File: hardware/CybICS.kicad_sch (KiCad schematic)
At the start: 64 parts, among them J1 Raspberry_Pi_2_3, J2 Conn_01x03_Pin, J3 Conn_01x05_Pin, SW1 SW_Push, SW2 SW_Push, U1 STM32G070RBTx

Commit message: Update on shematic and pcb design
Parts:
- C1, C2, C4: JLCPCB Part # (none) -> C38141
- C3: JLCPCB Part # (none) -> C1779
- D1, D14, D16, D18, D5, D6: JLCPCB Part # (none) -> C434438
- D10, D3: JLCPCB Part # (none) -> C434440
- D11, D12, D13, D15, D17, D19, D2, D4, D8: JLCPCB Part # (none) -> C434442
- D7, D9: JLCPCB Part # (none) -> C434441
- DS1: JLCPCB Part # (none) -> C5307341
- J1: JLCPCB Part # (none) -> C5224014
- J2: JLCPCB Part # (none) -> C168677
- J3: JLCPCB Part # (none) -> C225257
- R1, R10, R11, R12, R2, R20, R21, R22, R23, R24, R25, R26, R3, R4, R5, R6, R7, R8, R9: JLCPCB Part # (none) -> C17408
- R13, R14, R15, R16, R17, R18, R19: JLCPCB Part # (none) -> C304192
- R27: JLCPCB Part # (none) -> C17513
- RV1: JLCPCB Part # (none) -> C36376
- SW1, SW2: JLCPCB Part # (none) -> C428628
- U1: JLCPCB Part # (none) -> C529340

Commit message: first rapid prototype phase finished
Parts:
- FID1, FID2, FID3, H1, H2, H3: now left out of the parts list
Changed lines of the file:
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@@
     )
   )
-  (symbol (lib_id "Mechanical:Fiducial") (at 16.51 190.5 0) (unit 1)
-    (in_bom yes) (on_board yes) (dnp no) (fields_autoplaced)
+  (symbol (lib_name "Fiducial_1") (lib_id "Mechanical:Fiducial") (at 16.51 190.5 0) (unit 1)
+    (in_bom no) (on_board yes) (dnp no) (fields_autoplaced)
     (property "Reference" "FID1" (at 19.05 189.23 0)
       (effects (font (size 1.27 1.27)) (justify left))
@@
   )
   (symbol (lib_id "Mechanical:MountingHole") (at 35.56 175.26 0) (unit 1)
-    (in_bom yes) (on_board yes) (dnp no) (fields_autoplaced)
+    (in_bom no) (on_board yes) (dnp no) (fields_autoplaced)
     (property "Reference" "H2" (at 38.1 173.99 0)
       (effects (font (size 1.27 1.27)) (justify left))
@@
   )
   (symbol (lib_id "Mechanical:MountingHole") (at 16.51 175.26 0) (unit 1)
-    (in_bom yes) (on_board yes) (dnp no) (fields_autoplaced)
+    (in_bom no) (on_board yes) (dnp no) (fields_autoplaced)
     (property "Reference" "H1" (at 19.05 173.99 0)
       (effects (font (size 1.27 1.27)) (justify left))
@@
   )
   (symbol (lib_id "Mechanical:MountingHole") (at 16.51 182.88 0) (unit 1)
-    (in_bom yes) (on_board yes) (dnp no) (fields_autoplaced)
+    (in_bom no) (on_board yes) (dnp no) (fields_autoplaced)
     (property "Reference" "H3" (at 19.05 181.61 0)
       (effects (font (size 1.27 1.27)) (justify left))
@@
   )
   (symbol (lib_id "Mechanical:Fiducial") (at 44.45 190.5 0) (unit 1)
-    (in_bom yes) (on_board yes) (dnp no) (fields_autoplaced)
+    (in_bom no) (on_board yes) (dnp no) (fields_autoplaced)
     (property "Reference" "FID3" (at 46.99 189.23 0)
       (effects (font (size 1.27 1.27)) (justify left))
@@
     )
   )
-  (symbol (lib_id "Mechanical:Fiducial") (at 30.48 190.5 0) (unit 1)
-    (in_bom yes) (on_board yes) (dnp no) (fields_autoplaced)
+  (symbol (lib_name "Fiducial_2") (lib_id "Mechanical:Fiducial") (at 30.48 190.5 0) (unit 1)
+    (in_bom no) (on_board yes) (dnp no) (fields_autoplaced)
     (property "Reference" "FID2" (at 33.02 189.23 0)
       (effects (font (size 1.27 1.27)) (justify left))

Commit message: Added vscode
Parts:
- J3: JLCPCB Part # C225257 -> C225480
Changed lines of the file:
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@@
       (effects (font (size 1.27 1.27)) hide)
     )
-    (property "JLCPCB Part #" "C225257" (at 266.7 152.4 0)
+    (property "JLCPCB Part #" "C225480" (at 266.7 152.4 0)
       (effects (font (size 1.27 1.27)) hide)
     )

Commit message: 5V to 1602
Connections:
- net +3V3: no longer DS1.2 (VDD)
- net +5V: now reaches J1.2 (5V)
- net +5V: now also DS1.2 (VDD), J1.4 (5V)
- no-connect marks 42 -> 40
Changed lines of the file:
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@@
   (junction (at 156.21 100.33) (diameter 0) (color 0 0 0 0)
   )
+  (junction (at 161.29 34.29) (diameter 0) (color 0 0 0 0)
+  )
   (junction (at 166.37 100.33) (diameter 0) (color 0 0 0 0)
   )
@@
   (no_connect (at 46.99 52.07))
   (no_connect (at 77.47 85.09))
-  (no_connect (at 163.83 34.29))
   (no_connect (at 186.69 87.63))
   (no_connect (at 46.99 97.79))
@@
   (no_connect (at 46.99 120.65))
   (no_connect (at 46.99 110.49))
-  (no_connect (at 161.29 34.29))
   (no_connect (at 146.05 62.23))
   (no_connect (at 186.69 80.01))
@@
     (stroke (width 0) (type default))
   )
+  (wire (pts (xy 161.29 27.94) (xy 161.29 34.29))
+    (stroke (width 0) (type default))
+  )
   (wire (pts (xy 92.71 153.67) (xy 95.25 153.67))
     (stroke (width 0) (type default))
   )
+  (wire (pts (xy 161.29 34.29) (xy 163.83 34.29))
+    (stroke (width 0) (type default))
+  )
   (wire (pts (xy 254 46.99) (xy 261.62 46.99))
     (stroke (width 0) (type default))
@@
     (stroke (width 0) (type default))
   )
-  (wire (pts (xy 243.84 30.48) (xy 243.84 34.29))
-    (stroke (width 0) (type default))
-  )
   (wire (pts (xy 80.01 31.75) (xy 80.01 33.02))
     (stroke (width 0) (type default))
@@
     (stroke (width 0) (type default))
   )
+  (wire (pts (xy 243.84 27.94) (xy 243.84 34.29))
+    (stroke (width 0) (type default))
+  )
   (wire (pts (xy 31.75 64.77) (xy 46.99 64.77))
     (stroke (width 0) (type default))
@@
     )
   )
+  (symbol (lib_id "power:+5V") (at 243.84 27.94 0) (unit 1)
+    (in_bom yes) (on_board yes) (dnp no) (fields_autoplaced)
+    (property "Reference" "#PWR09" (at 243.84 31.75 0)
+      (effects (font (size 1.27 1.27)) hide)
+    )
+    (property "Value" "+5V" (at 243.84 22.86 0)
+      (effects (font (size 1.27 1.27)))
+    )
+    (property "Footprint" "" (at 243.84 27.94 0)
+      (effects (font (size 1.27 1.27)) hide)
+    )
+    (property "Datasheet" "" (at 243.84 27.94 0)
+      (effects (font (size 1.27 1.27)) hide)
+    )
+    (pin "1")
+    (instances
+      (project "CybICS"
+        (path "/8fcde287-628f-41a4-bd3a-47641b4dabbc"
+          (reference "#PWR09") (unit 1)
+        )
+      )
+    )
+  )
   (symbol (lib_id "Switch:SW_Push") (at 123.19 186.69 90) (unit 1)
     (in_bom yes) (on_board yes) (dnp no) (fields_autoplaced)
@@
     )
   )
-  (symbol (lib_id "power:+3V3") (at 243.84 30.48 0) (unit 1)
-    (in_bom yes) (on_board yes) (dnp no) (fields_autoplaced)
-    (property "Reference" "#PWR09" (at 243.84 34.29 0)
-      (effects (font (size 1.27 1.27)) hide)
-    )
-    (property "Value" "+3V3" (at 243.84 25.4 0)
-      (effects (font (size 1.27 1.27)))
-    )
-    (property "Footprint" "" (at 243.84 30.48 0)
-      (effects (font (size 1.27 1.27)) hide)
-    )
-    (property "Datasheet" "" (at 243.84 30.48 0)
-      (effects (font (size 1.27 1.27)) hide)
-    )
-    (pin "1")
-    (instances
-      (project "CybICS"
-        (path "/8fcde287-628f-41a4-bd3a-47641b4dabbc"
-          (reference "#PWR09") (unit 1)
-        )
-      )
-    )
-  )
   (symbol (lib_id "power:+3V3") (at 208.28 132.08 0) (unit 1)
     (in_bom yes) (on_board yes) (dnp no) (fields_autoplaced)
@@
         )
       )
+    )
+  )
+  (symbol (lib_id "power:+5V") (at 161.29 27.94 0) (unit 1)
+    (in_bom yes) (on_board yes) (dnp no) (fields_autoplaced)
+    (property "Reference" "#PWR040" (at 161.29 31.75 0)
+      (effects (font (size 1.27 1.27)) hide)
+    )
+    (property "Value" "+5V" (at 161.29 22.86 0)
+      (effects (font (size 1.27 1.27)))
+    )
+    (property "Footprint" "" (at 161.29 27.94 0)
+      (effects (font (size 1.27 1.27)) hide)
+    )
+    (property "Datasheet" "" (at 161.29 27.94 0)
+      (effects (font (size 1.27 1.27)) hide)
+    )
+    (pin "1")
+    (instances
+      (project "CybICS"
+        (path "/8fcde287-628f-41a4-bd3a-47641b4dabbc"
+          (reference "#PWR040") (unit 1)
+        )
+      )

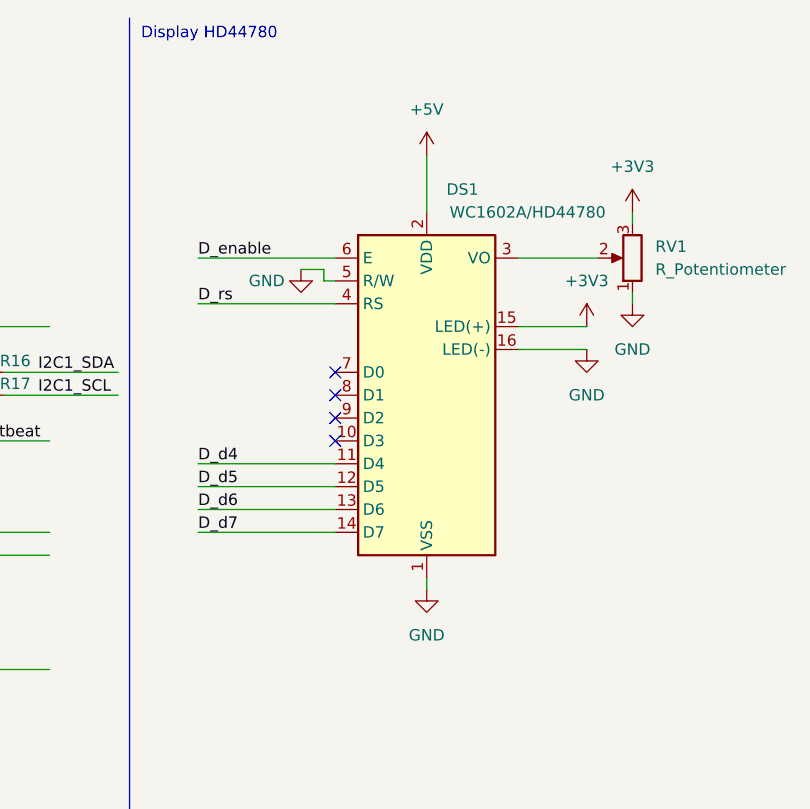
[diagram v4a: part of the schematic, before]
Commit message: Added pwr flag
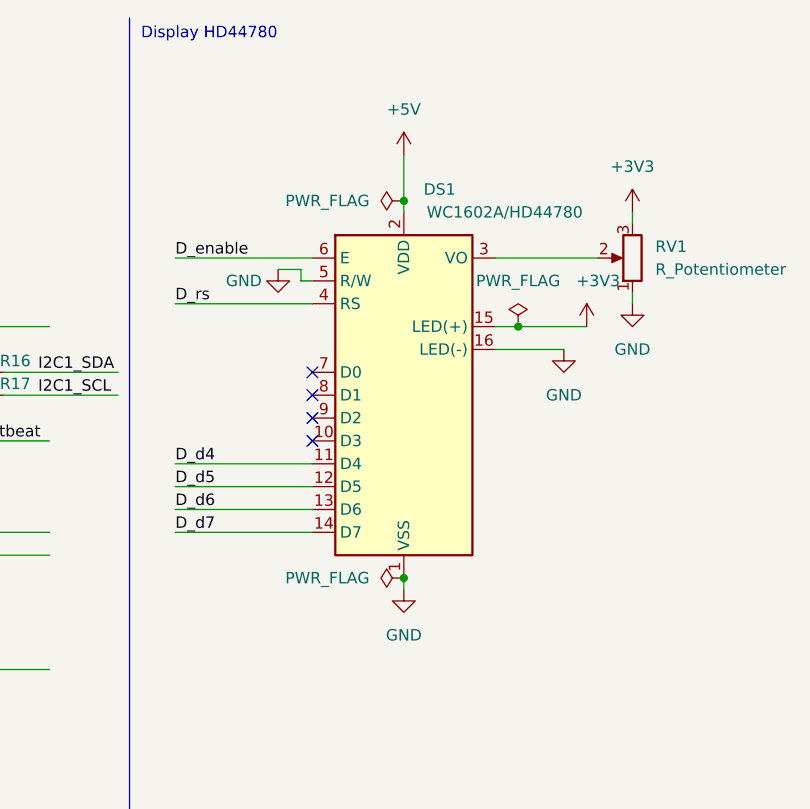
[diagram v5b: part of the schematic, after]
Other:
- moved on the sheet: DS1
